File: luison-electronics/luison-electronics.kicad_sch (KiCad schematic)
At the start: 30 parts, among them SW1 SW_DIP_x06, SW2 SW_Push, U1 YAAJ_DCDC_StepDown_LM2596

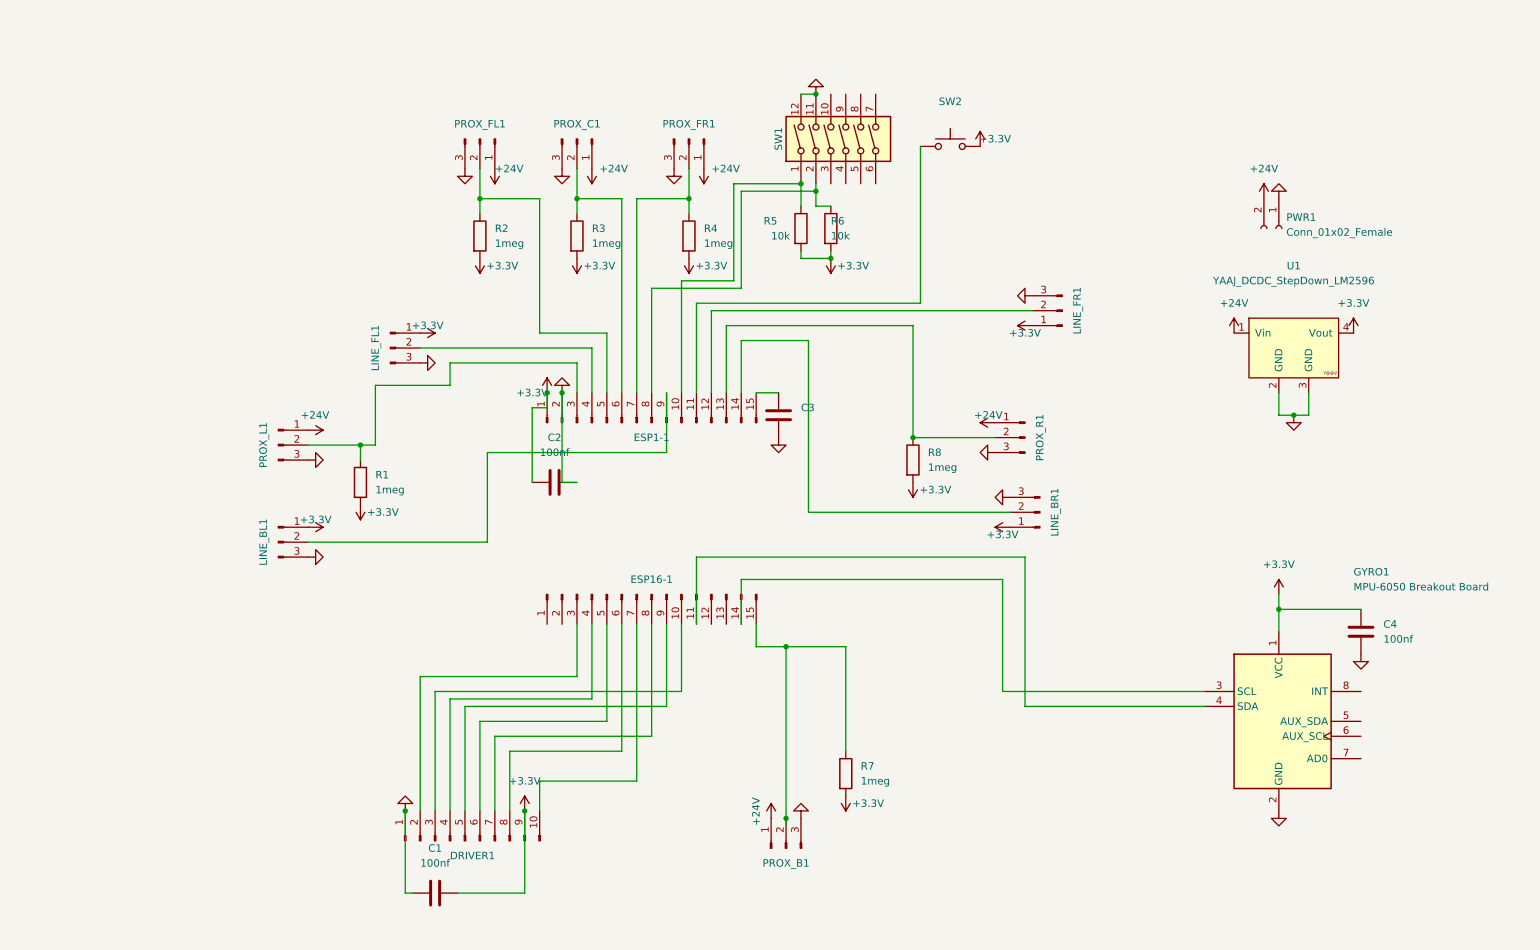
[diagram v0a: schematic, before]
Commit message: Finish schematic and place components in pcb
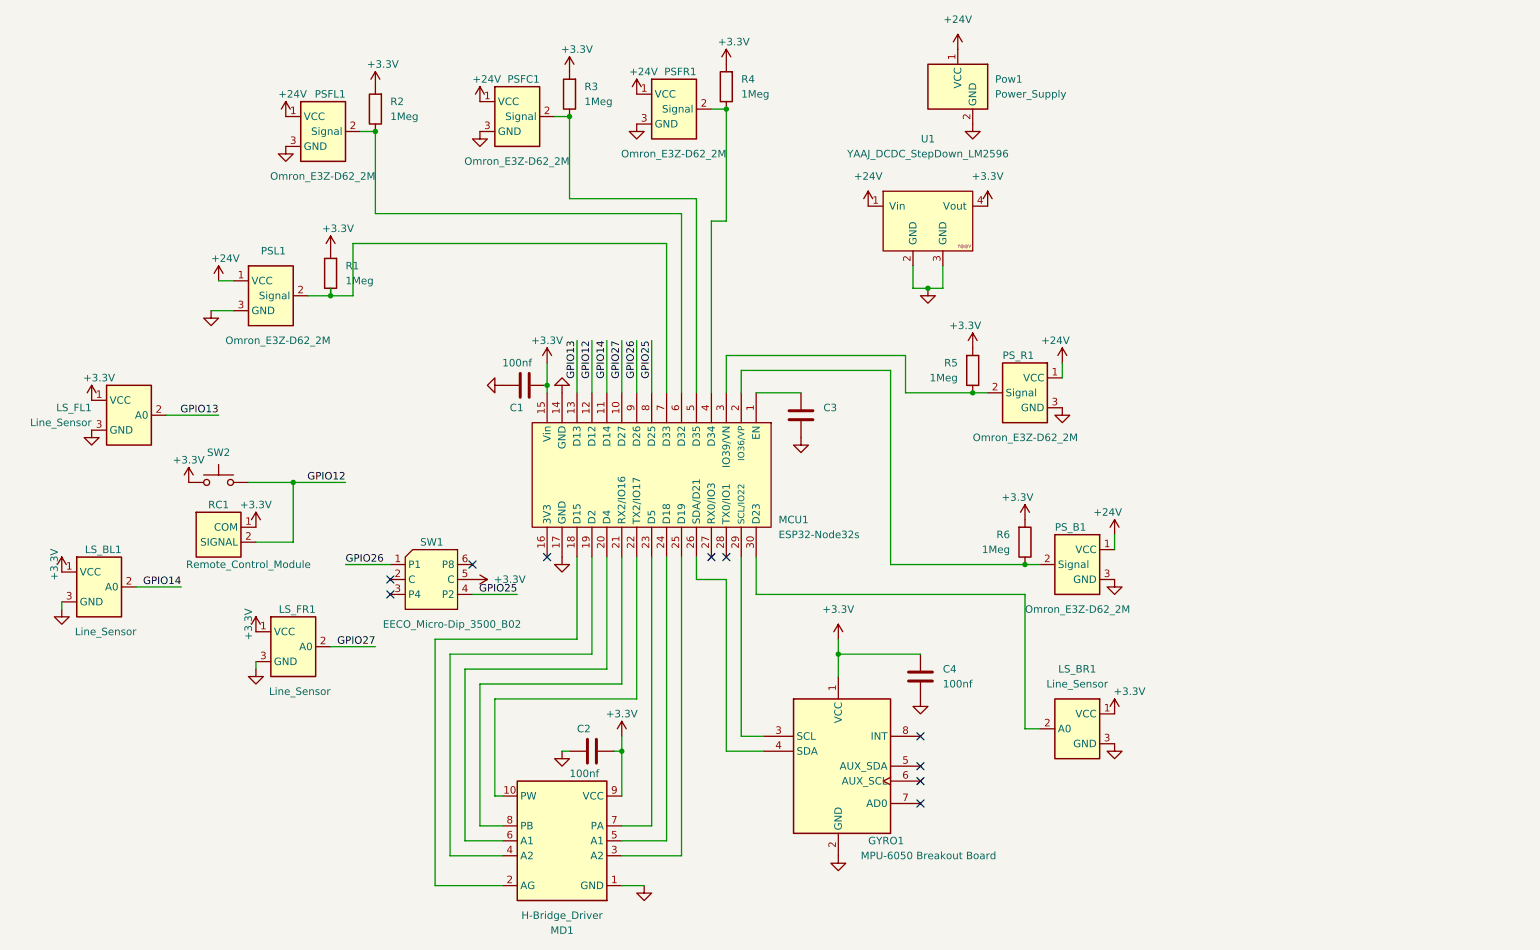
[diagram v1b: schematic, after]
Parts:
- removed DRIVER1: Conn_01x10_Male, Connector_PinHeader_2.54mm:PinHeader_2x05_P2.54mm_Vertical, symbol Connector:Conn_01x10_Male
- removed ESP1-1, ESP16-1: Conn_01x15_Male, Connector_PinSocket_2.54mm:PinSocket_1x15_P2.54mm_Vertical, symbol Connector:Conn_01x15_Male
- removed LINE_BL1, LINE_BR1, LINE_FL1, LINE_FR1, PROX_B1, PROX_C1, PROX_FL1, PROX_FR1, PROX_L1, PROX_R1: Conn_01x03_Male, TerminalBlock:TerminalBlock_bornier-3_P5.08mm, symbol Connector:Conn_01x03_Male
- removed PWR1: Conn_01x02_Female, TerminalBlock:TerminalBlock_bornier-2_P5.08mm, symbol Connector:Conn_01x02_Female
- removed R7, R8: 1meg, Resistor_THT:R_Axial_DIN0207_L6.3mm_D2.5mm_P7.62mm_Horizontal, symbol Device:R
- removed SW1: SW_DIP_x06, Button_Switch_THT:SW_DIP_SPSTx06_Slide_9.78x17.42mm_W7.62mm_P2.54mm, symbol Switch:SW_DIP_x06
- added LS_BL1, LS_BR1, LS_FL1, LS_FR1: Line_Sensor, TerminalBlock:TerminalBlock_bornier-3_P5.08mm, symbol luison-electronics:Line_Sensor
- added MCU1: ESP32-Node32s, luison-electronics:ESP32-Node32s, symbol luison-electronics:ESP32-Node32s
- added MD1: H-Bridge_Driver, Connector_PinHeader_2.54mm:PinHeader_2x05_P2.54mm_Vertical, symbol luison-electronics:H-Bridge_Driver
- added PSFC1, PSFL1, PSFR1, PSL1, PS_B1, PS_R1: Omron_E3Z-D62_2M, TerminalBlock:TerminalBlock_bornier-3_P5.08mm, symbol luison-electronics:Omron_E3Z-D62_2M
- added Pow1: Power_Supply, TerminalBlock:TerminalBlock_bornier-2_P5.08mm, symbol luison-electronics:Power_Supply
- added RC1: Remote_Control_Module, TerminalBlock:TerminalBlock_bornier-2_P5.08mm, symbol luison-electronics:Remote_Control_Module
- added SW1: EECO_Micro-Dip_3500_B02, luison-electronics:EECO Rotary Switch, symbol luison-electronics:EECO_Micro-Dip_3500_B02
- GYRO1: footprint luison-electronics:MPU6050 Breakout Board -> keilev_Library:MPU6050 Breakout Board
- R1, R2, R3, R4: value 1meg -> 1Meg
- R5, R6: value 10k -> 1Meg
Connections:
- net +24V: now also PSFC1.1 (VCC), PSFL1.1 (VCC), PSFR1.1 (VCC), PSL1.1 (VCC), PS_B1.1 (VCC), PS_R1.1 (VCC), Pow1.1 (VCC)
- net +3.3V: now also C2.2, SW2.1, LS_BL1.1 (VCC), LS_BR1.1 (VCC), LS_FL1.1 (VCC), LS_FR1.1 (VCC), MCU1.15 (Vin), MD1.9 (VCC), RC1.1 (COM), SW1.5 (C); no longer C2.1, SW2.2
- net GND: now also C2.1, LS_BL1.3 (GND), LS_BR1.3 (GND), LS_FL1.3 (GND), LS_FR1.3 (GND), MCU1.14 (GND), MCU1.17 (GND), MD1.1 (GND), PSFC1.3 (GND), PSFL1.3 (GND), PSFR1.3 (GND), PSL1.3 (GND), PS_B1.3 (GND), PS_R1.3 (GND), Pow1.2 (GND); no longer C2.2
- net at R4.1: now also MCU1.4 (D34), PSFR1.2 (Signal)
- net at GYRO1.3 (SCL): now also MCU1.29 (SCL/IO22)
- net at GYRO1.4 (SDA): now also MCU1.26 (SDA/D21)
- net at R5.1: now also MCU1.3 (IO39/VN), PS_R1.2 (Signal)
- net at R6.1: now also MCU1.2 (IO36/VP), PS_B1.2 (Signal)
- net at R1.1: now also MCU1.7 (D33), PSL1.2 (Signal)
- net at R3.1: now also MCU1.5 (D35), PSFC1.2 (Signal)
- net at C3.1: now also MCU1.1 (EN)
- net at R2.1: now also MCU1.6 (D32), PSFL1.2 (Signal)
- new net: LS_BR1.2 (A0), MCU1.30 (D23)
- new net: MCU1.22 (TX2/IO17), MD1.10 (PW)
- new net: MCU1.18 (D15), MD1.2 (AG)
- new net: MCU1.25 (D19), MD1.3 (A2)
- new net: MCU1.19 (D2), MD1.4 (A2)
- new net: MCU1.24 (D18), MD1.5 (A1)
- new net: MCU1.20 (D4), MD1.6 (A1)
- new net: MCU1.23 (D5), MD1.7 (PA)
- new net: MCU1.21 (RX2/IO16), MD1.8 (PB)
- new net GPIO12: MCU1.12 (D12), RC1.2 (SIGNAL), SW2.2
- new net GPIO13: LS_FL1.2 (A0), MCU1.13 (D13)
- new net GPIO14: LS_BL1.2 (A0), MCU1.11 (D14)
- new net GPIO25: MCU1.8 (D25), SW1.4 (P2)
- new net GPIO26: MCU1.9 (D26), SW1.1 (P1)
- new net GPIO27: LS_FR1.2 (A0), MCU1.10 (D27)
- no-connect marks 0 -> 10
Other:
- moved on the sheet: C3, C4, GYRO1, R1, U1

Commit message: Finish dual layer PCB and generate manufacture job files
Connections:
- net GPIO12: now also LS_FR1.2 (A0); no longer RC1.2 (SIGNAL), SW2.2
- net GPIO14: now also RC1.2 (SIGNAL), SW2.2; no longer LS_BL1.2 (A0)
- net GPIO27: now also LS_BL1.2 (A0); no longer LS_FR1.2 (A0)
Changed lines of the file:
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@@
     (stroke (width 0) (type default) (color 0 0 0 0))
   )
-  (wire (pts (xy 73.66 125.73) (xy 66.04 125.73))
+  (wire (pts (xy 76.2 125.73) (xy 66.04 125.73))
     (stroke (width 0) (type default) (color 0 0 0 0))
   )
@@
     (effects (font (size 1.27 1.27)) (justify right bottom))
   )
-  (label "GPIO14" (at 40.64 115.57 180)
+  (label "GPIO27" (at 40.64 115.57 180)
     (effects (font (size 1.27 1.27)) (justify right bottom))
   )
@@
     (effects (font (size 1.27 1.27)) (justify right bottom))
   )
-  (label "GPIO12" (at 68.58 97.79 180)
+  (label "GPIO14" (at 68.58 97.79 180)
     (effects (font (size 1.27 1.27)) (justify right bottom))
   )
@@
     (effects (font (size 1.27 1.27)) (justify right bottom))
   )
-  (label "GPIO27" (at 73.66 125.73 180)
+  (label "GPIO12" (at 76.2 125.73 180)
     (effects (font (size 1.27 1.27)) (justify right bottom))
   )

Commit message: Add new symbols in schematic and new layout of pcb
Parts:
- added GYRO2: MPU-6050 Breakout Board, keilev_Library:MPU6050 Breakout Board, symbol keilev_Library:MPU-6050 Breakout Board
- added LS1, LS2, LS3, LS4: Line_Sensor, luison-electronics:JST_XH_B3B-XH-A_1x03_P2.50mm_Vertical, symbol luison-electronics:Line_Sensor
- added MCU2: ESP32-S2-DevKitC-1, luison-electronics:ESP32-S2-DevKitC-1, symbol luison-electronics:ESP32-S2-DevKitC-1
- added MD2: RoboClaw ST 2x45A Motor Controller, symbol luison-electronics:RoboClaw ST 2x45A Motor Controller
- added PS1, PS2, PS3, PS4, PS5, PS6: Omron_E3Z-D62_2M, luison-electronics:JST_XH_B3B-XH-A_1x03_P2.50mm_Vertical, symbol luison-electronics:Omron_E3Z-D62_2M
- added SW3: EECO_Micro-Dip_3500_B02, luison-electronics:EECO Rotary Switch, symbol luison-electronics:EECO_Micro-Dip_3500_B02
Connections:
- net +24V: now also PS1.1 (VCC), PS2.1 (VCC), PS3.1 (VCC), PS4.1 (VCC), PS5.1 (VCC), PS6.1 (VCC)
- net +3.3V: now also GYRO2.1 (VCC), LS1.1 (VCC), LS2.1 (VCC), LS3.1 (VCC), LS4.1 (VCC), MCU2.1 (3V3), MCU2.2 (3V3), SW3.2 (C), SW3.5 (C)
- net GND: now also GYRO2.2 (GND), LS1.3 (GND), LS2.3 (GND), LS3.3 (GND), LS4.3 (GND), MCU2.22 (GND), MCU2.23 (GND), MCU2.43 (GND), MCU2.44 (GND), MD2.6 (GND), PS1.3 (GND), PS2.3 (GND), PS3.3 (GND), PS4.3 (GND), PS5.3 (GND), PS6.3 (GND)
- new net +5V: MCU2.21 (5V), MD2.7 (+5V)
- new net LS_BL: LS2.2 (A0), MCU2.27 (IO2/ADC)
- new net LS_BR: LS4.2 (A0), MCU2.26 (IO1/ADC)
- new net LS_FL: LS1.2 (A0), MCU2.6 (IO6/ADC)
- new net LS_FR: LS3.2 (A0), MCU2.5 (IO5/ADC)
- new net PS_B: MCU2.39 (IO33), PS5.2 (Signal)
- new net PS_FC: MCU2.18 (IO12/ADC), PS2.2 (Signal)
- new net PS_FL: MCU2.19 (IO13/ADC), PS1.2 (Signal)
- new net PS_FR: MCU2.17 (IO11/ADC), PS3.2 (Signal)
- new net PS_L: MCU2.40 (IO21), PS4.2 (Signal)
- new net PS_R: MCU2.38 (IO34), PS6.2 (Signal)
- new net RX1_MD: MCU2.11 (IO18/ADC/DAC), MD2.2 (S2/TX)
- new net SCL: GYRO2.3 (SCL), MCU2.15 (IO9/ADC)
- new net SDA: GYRO2.4 (SDA), MCU2.12 (IO8/ADC)
- new net SW_P1: SW3.1 (P1)
- new net SW_P2: SW3.4 (P2)
- new net SW_P4: SW3.3 (P4)
- new net SW_P8: SW3.6 (P8)
- new net TX1_MD: MCU2.10 (IO17/ADC/DAC), MD2.1 (S1/RX)
- no-connect marks 10 -> 14
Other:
- note added: "Acelerómetro"
- note added: "Dip Switch Rotatorio"
- note added: "Driver"
- note added: "Sensores de Línea"
- note added: "Sensores de Proximidad"
- moved on the sheet: C1, C2, C3, C4, GYRO1, LS_BL1, LS_BR1, LS_FL1, LS_FR1, MCU1, MD1, PSFC1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

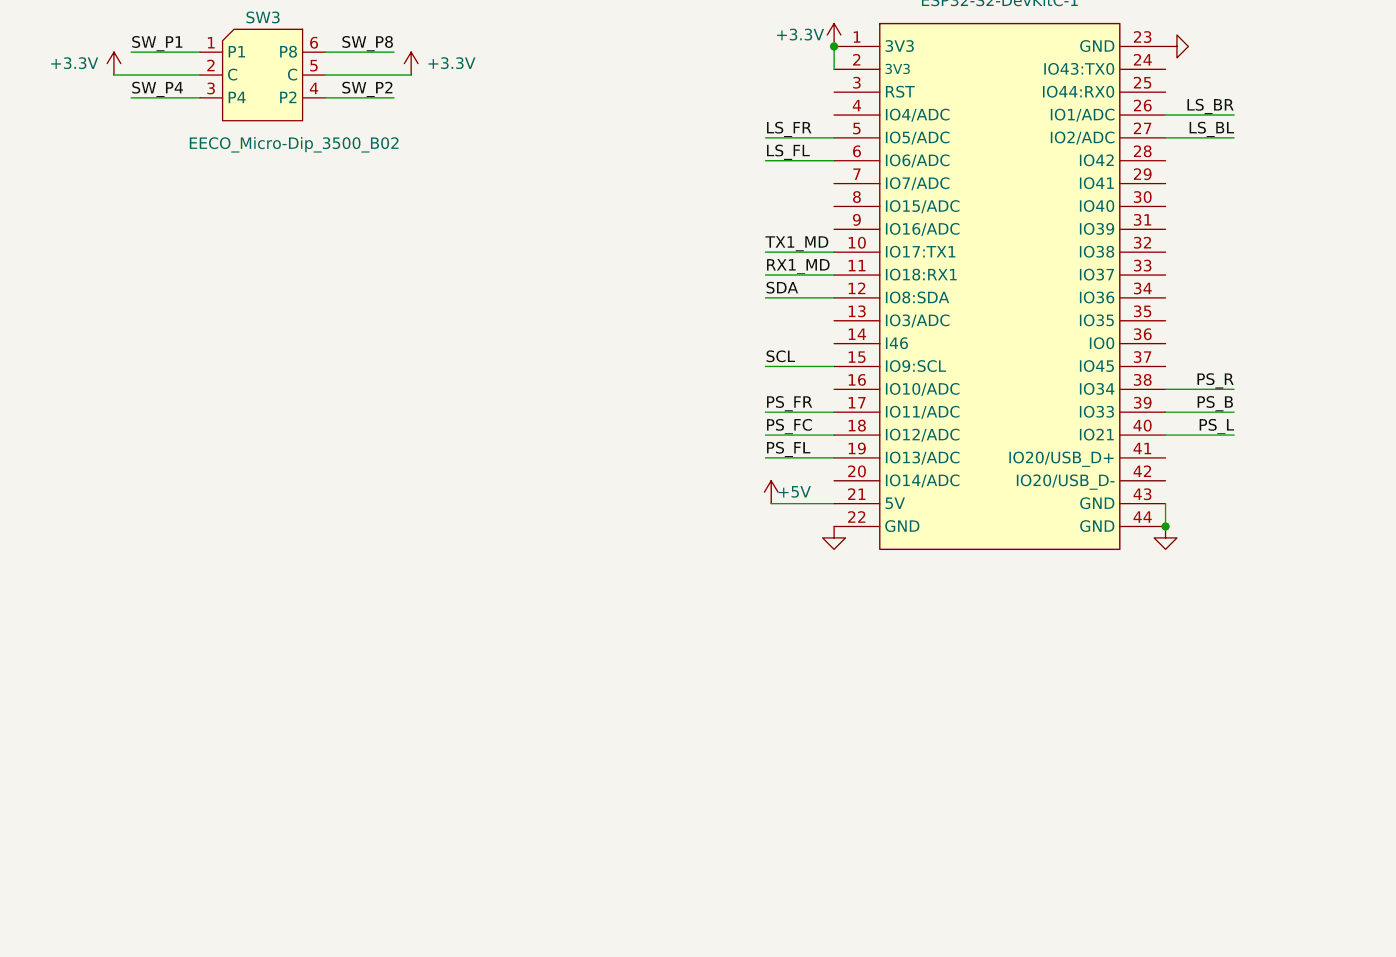
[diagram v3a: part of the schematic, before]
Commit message: Add killlswitch library and layout pcb components
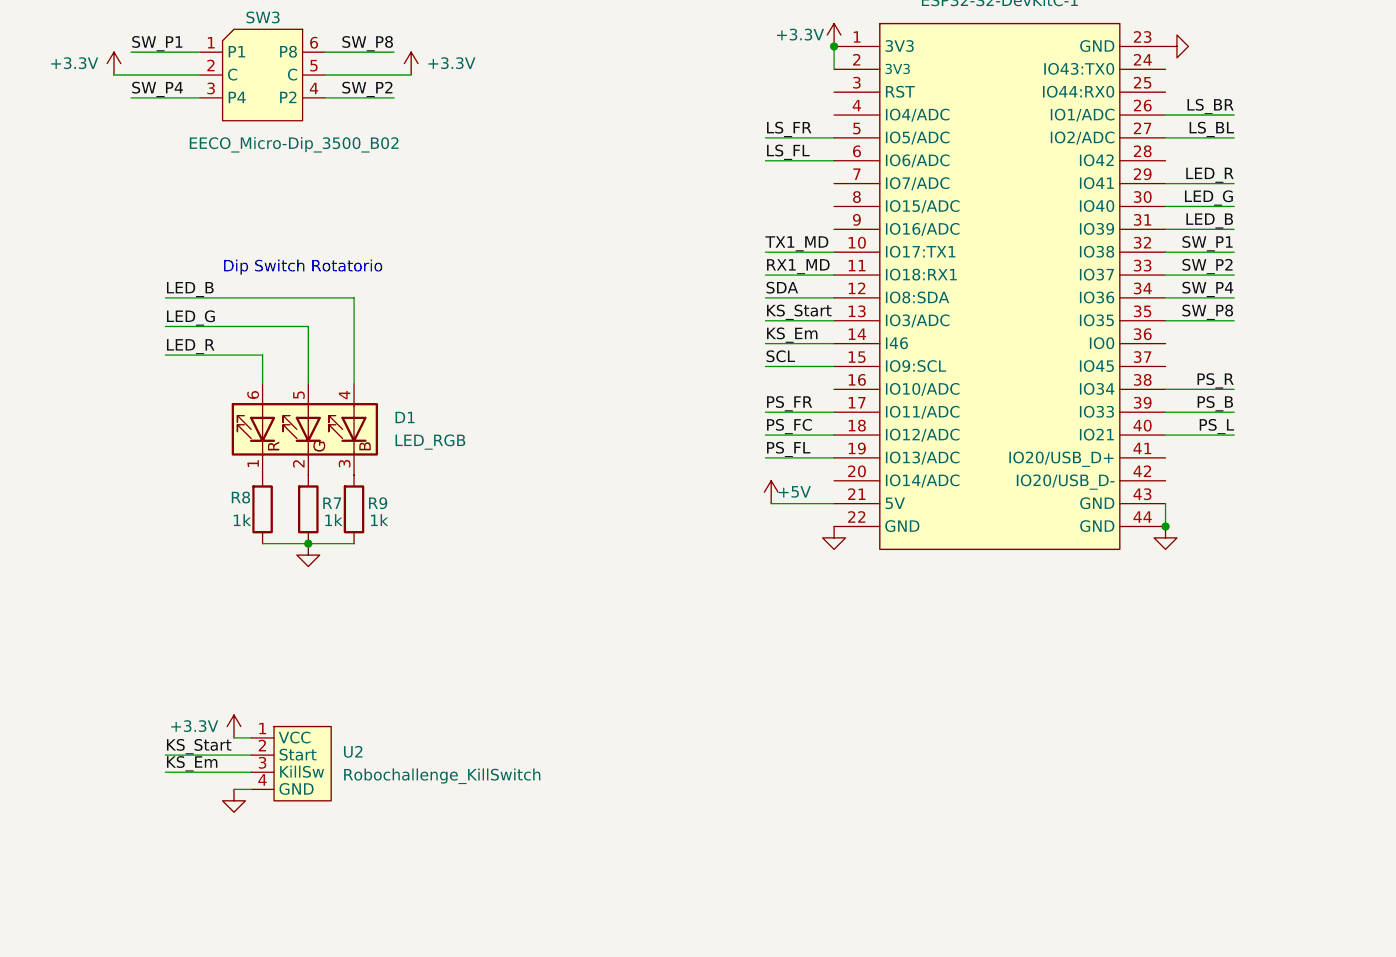
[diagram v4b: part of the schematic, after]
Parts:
- added D1: LED_RGB, LED_THT:LED_D5.0mm-4_RGB, symbol Device:LED_RGB
- added R7, R8, R9: 1k, Resistor_THT:R_Axial_DIN0207_L6.3mm_D2.5mm_P7.62mm_Horizontal, symbol Device:R
- added U2: Robochallenge_KillSwitch, luison-electronics:Robochallenge_KillSwitch, symbol luison-electronics:Robochallenge_KillSwitch
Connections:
- net +3.3V: now also U2.1 (VCC)
- net GND: now also R7.1, R8.1, R9.1, U2.4 (GND)
- net SW_P1: now also MCU2.32 (IO38)
- net SW_P2: now also MCU2.33 (IO37)
- net SW_P4: now also MCU2.34 (IO36)
- net SW_P8: now also MCU2.35 (IO35)
- net KS_Start: now reaches MCU2.13 (IO3/ADC)
- net KS_Start: now also U2.2 (Start)
- net KS_Em: now reaches MCU2.14 (I46)
- net KS_Em: now also U2.3 (KillSw)
- net LED_R: now reaches MCU2.29 (IO41)
- net LED_R: now also D1.6 (RA)
- net LED_G: now reaches MCU2.30 (IO40)
- net LED_G: now also D1.5 (GA)
- net LED_B: now reaches MCU2.31 (IO39)
- net LED_B: now also D1.4 (BA)
- new net: D1.3 (BK), R9.2
- new net: D1.2 (GK), R8.2
- new net: D1.1 (RK), R7.2

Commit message: Creacion de nueva placa
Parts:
- removed D1: LED_RGB, LED_THT:LED_D5.0mm-4_RGB, symbol Device:LED_RGB
- removed R7, R8, R9: 1k, Resistor_THT:R_Axial_DIN0207_L6.3mm_D2.5mm_P7.62mm_Horizontal, symbol Device:R
- added PS7: conector_driver, luison-electronics:JST_XH_B3B-XH-A_1x03_P2.50mm_Vertical, symbol luison-electronics:Omron_E3Z-D62_2M
- added PS8, PS9: alimentacion_driver, luison-electronics:JST_XH_B3B-XH-A_1x03_P2.50mm_Vertical, symbol luison-electronics:Omron_E3Z-D62_2M
- GYRO2: footprint keilev_Library:MPU6050 Breakout Board -> luison-electronics:MPU6050 Breakout Board
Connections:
- net LED_B is gone; now on net SW_P8: MCU2.31 (IO39)
- net LED_G is gone; now on net SW_P2: MCU2.30 (IO40)
- net +24V: now also PS9.3 (24V)
- net +5V: now also PS9.1 (5V)
- net GND: now also PS9.2 (GND)
- net LS_BL: now also MCU2.5 (IO5/ADC); no longer MCU2.27 (IO2/ADC)
- net LS_BR: now also MCU2.28 (IO42); no longer MCU2.26 (IO1/ADC)
- net LS_FL: now also MCU2.3 (RST); no longer MCU2.6 (IO6/ADC)
- net LS_FR: now also MCU2.24 (IO43); no longer MCU2.5 (IO5/ADC)
- net PS_B: now also MCU2.41 (IO20/USB_D+); no longer MCU2.39 (IO33)
- net PS_FC: now also MCU2.19 (IO13/ADC); no longer MCU2.18 (IO12/ADC)
- net PS_FL: now also MCU2.15 (IO9/ADC); no longer MCU2.19 (IO13/ADC)
- net PS_FR: now also MCU2.20 (IO14/ADC); no longer MCU2.17 (IO11/ADC)
- net PS_L: now also MCU2.37 (IO45); no longer MCU2.40 (IO21)
- net PS_R: now also MCU2.42 (IO20/USB_D-); no longer MCU2.38 (IO34)
- net RX1_MD: now also MCU2.10 (IO17/ADC/DAC), PS7.3 (RX); no longer MCU2.11 (IO18/ADC/DAC)
- net SCL: now also MCU2.26 (IO1/ADC); no longer MCU2.15 (IO9/ADC)
- net SDA: now also MCU2.25 (IO44); no longer MCU2.12 (IO8/ADC)
- net SW_P1: now also MCU2.34 (IO36); no longer MCU2.32 (IO38)
- net SW_P2: no longer MCU2.33 (IO37)
- net SW_P4: now also MCU2.33 (IO37); no longer MCU2.34 (IO36)
- net SW_P8: no longer MCU2.35 (IO35)
- net TX1_MD: now also MCU2.8 (IO15/ADC), PS7.1 (TX); no longer MCU2.10 (IO17/ADC/DAC)
- net 4: now reaches MCU2.4 (IO4/ADC)
- net 4: now also PS8.1 (5V)
- net 7: now reaches MCU2.7 (IO7/ADC)
- net 7: now also PS8.3 (24V)
- net KS_EM: now reaches MCU2.9 (IO16/ADC)
- net KS_EM: now also U2.3 (KillSw), PS7.2 (KS)
- net KS_Em: no longer names the net of MCU2.14 (I46)
- net KS_Em: no longer U2.3 (KillSw)
- net KS_Start: no longer names the net of MCU2.13 (IO3/ADC)
- net KS_Start: no longer U2.2 (Start)
- net LED_R: no longer names the net of MCU2.29 (IO41)
- new net 6: MCU2.6 (IO6/ADC), PS8.2 (GND)
- new net KS_START: MCU2.11 (IO18/ADC/DAC), U2.2 (Start)
